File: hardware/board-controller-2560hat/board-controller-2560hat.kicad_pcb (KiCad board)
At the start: 2 copper layers, 3 parts

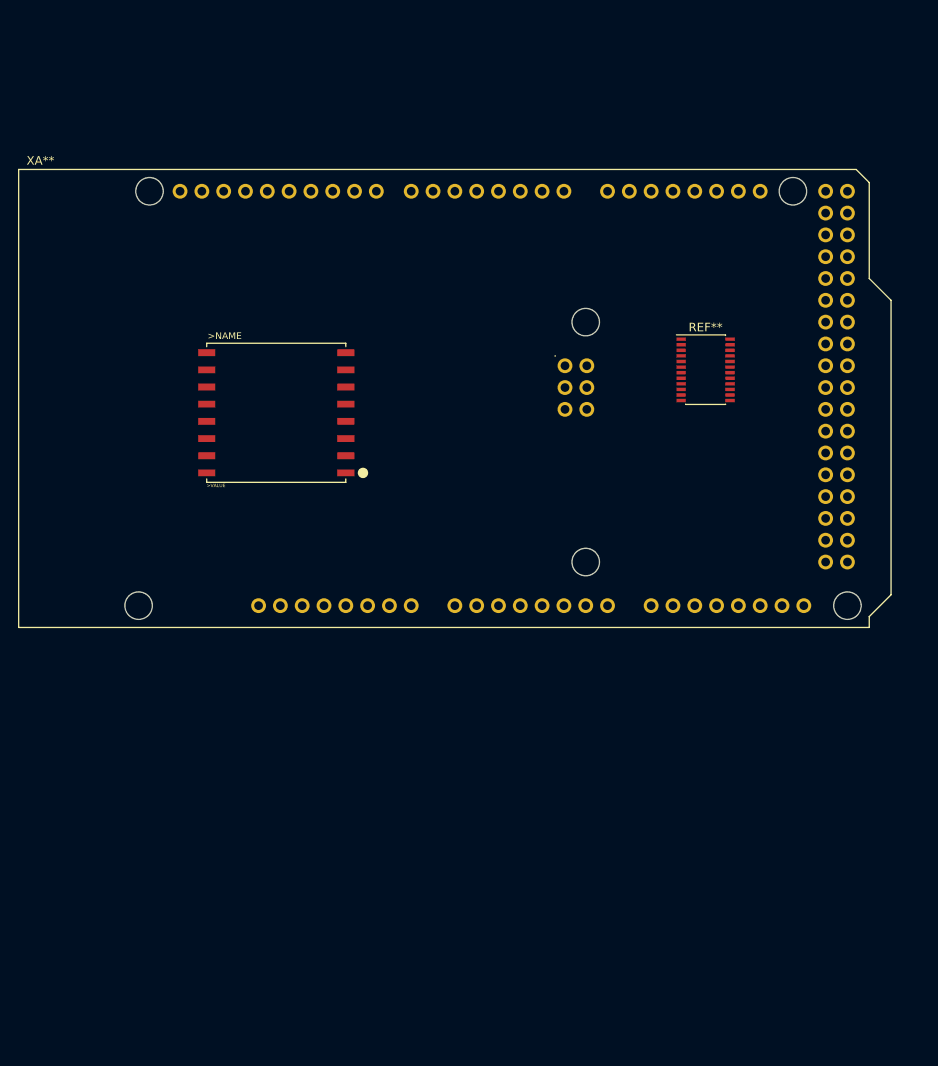
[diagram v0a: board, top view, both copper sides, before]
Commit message: Fixing TFT_ pinouts and rebuilding PCB
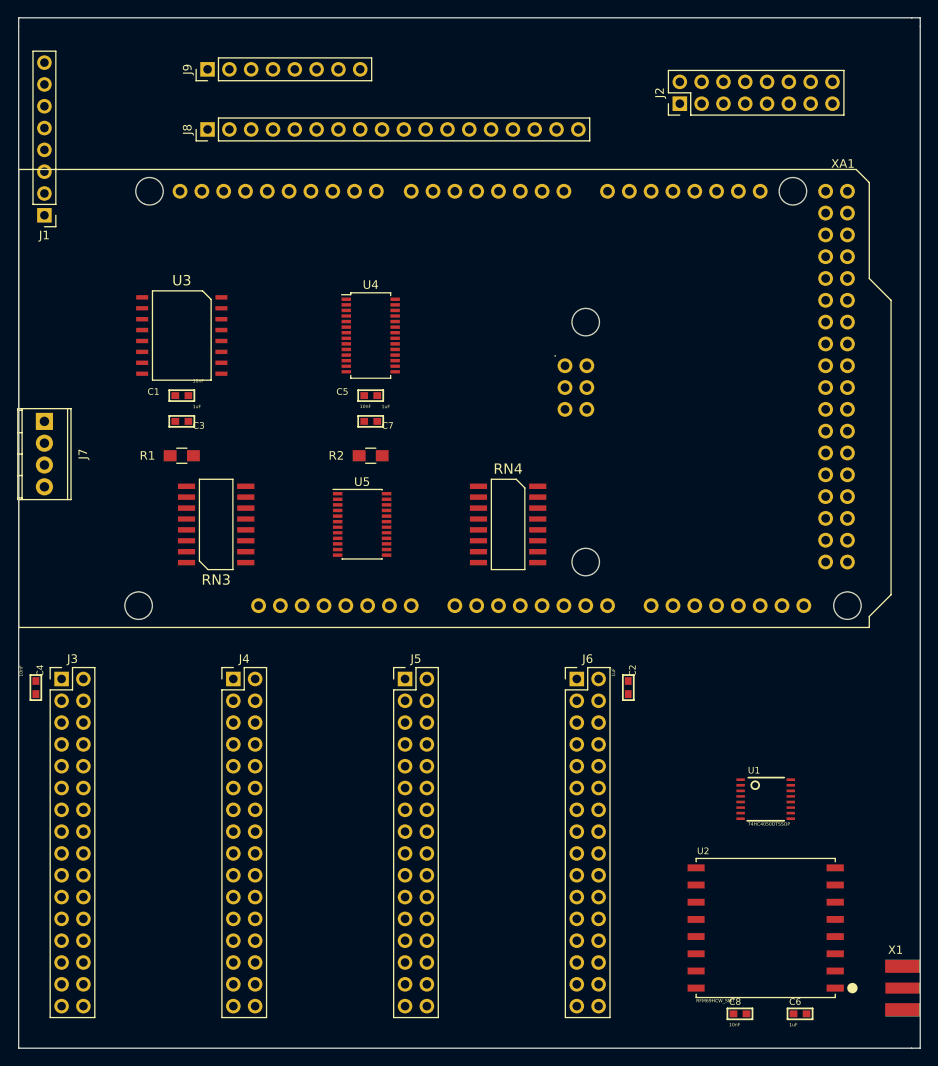
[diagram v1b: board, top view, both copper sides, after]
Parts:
- removed >NAME: >VALUE, Adafruit RFM+LoRa Breakout:RFMHCW_SMT
- removed REF**: TSSOP-24_4.4x7.8mm_Pitch0.65mm, Housings_SSOP:TSSOP-24_4.4x7.8mm_Pitch0.65mm
- removed XA**: Arduino_Mega2560_Shield, Arduino:Arduino_Mega2560_Shield
- added C1: 10nF, _0603, F.Cu at (114.0, 73.0)
- added C2: 1uF, _0603, F.Cu at (166.0, 107.0)
- added C3: 1uF, _0603, F.Cu at (114.0, 76.0)
- added C4: 10nF, _0603, F.Cu at (97.0, 107.0)
- added C5: 10nF, _0603, F.Cu at (136.0, 73.0)
- added C6: 1uF, _0603, F.Cu at (186.0, 145.0)
- added C7: 1uF, _0603, F.Cu at (136.0, 76.0)
- added C8: 10nF, _0603, F.Cu at (179.0, 145.0)
- added J1: CONN_POWER, Pin_Headers:Pin_Header_Straight_1x08_Pitch2.54mm, F.Cu at (98.0, 52.0)
- added J2: CONN_LCD, Pin_Headers:Pin_Header_Straight_2x08_Pitch2.54mm, F.Cu at (172.0, 39.0)
- added J3: CONN_BOARD0, Pin_Headers:Pin_Header_Straight_2x16_Pitch2.54mm, F.Cu at (100.0, 106.0)
- added J4: CONN_BOARD1, Pin_Headers:Pin_Header_Straight_2x16_Pitch2.54mm, F.Cu at (120.0, 106.0)
- added J5: CONN_BOARD2, Pin_Headers:Pin_Header_Straight_2x16_Pitch2.54mm, F.Cu at (140.0, 106.0)
- added J6: CONN_BOARD3, Pin_Headers:Pin_Header_Straight_2x16_Pitch2.54mm, F.Cu at (160.0, 106.0)
- added J7: CONN_SW, Connectors_Terminal_Blocks:TerminalBlock_Pheonix_MPT-2.54mm_4pol, F.Cu at (98.0, 76.0)
- added J8: CONN_KEYLED, Pin_Headers:Pin_Header_Straight_1x18_Pitch2.54mm, F.Cu at (117.0, 42.0)
- added J9: CONN_KEYSW, Pin_Headers:Pin_Header_Straight_1x08_Pitch2.54mm, F.Cu at (117.0, 35.0)
- added R1: 2k2, Resistors_SMD:R_0805_HandSoldering, F.Cu at (114.0, 80.0)
- added R2: 2k2, Resistors_SMD:R_0805_HandSoldering, F.Cu at (136.0, 80.0)
- added RN3: 10k, Housings_SOIC:CA_SOIC_16_5.59x11.18_1.27_Pitch, F.Cu at (118.0, 88.0)
- added RN4: 10k, Housings_SOIC:CA_SOIC_16_5.59x11.18_1.27_Pitch, F.Cu at (152.0, 88.0)
- added U1: 74HC4050DTSSOP, TSSOP16, F.Cu at (182.0, 120.0)
- added U2: RFM69HCW_SMT, RFMHCW_SMT, F.Cu at (182.0, 135.0)
- added U3: PCF8574, Housings_SOIC:CA_SOIC_16_7.5x10.5_1.27_Pitch, F.Cu at (114.0, 66.0)
- added U4: PCA9635PW, Housings_SSOP:TSSOP-28_4.4x9.7mm_Pitch0.65mm, F.Cu at (136.0, 66.0)
- added U5: TCA9548A_TSSOP, Housings_SSOP:TSSOP-24_4.4x7.8mm_Pitch0.65mm, F.Cu at (135.0, 88.0)
- added X1: SMACONNECTOR_EDGE, SMA_EDGELAUNCH, F.Cu at (200.0, 142.0)
- added XA1: Arduino_Mega2560_Shield, Arduino:Arduino_Mega2560_Shield, F.Cu at (95.0, 100.0)
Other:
- board outline added: 105 x 120 mm

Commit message: Adding first autoroute - still need to check nets are correct
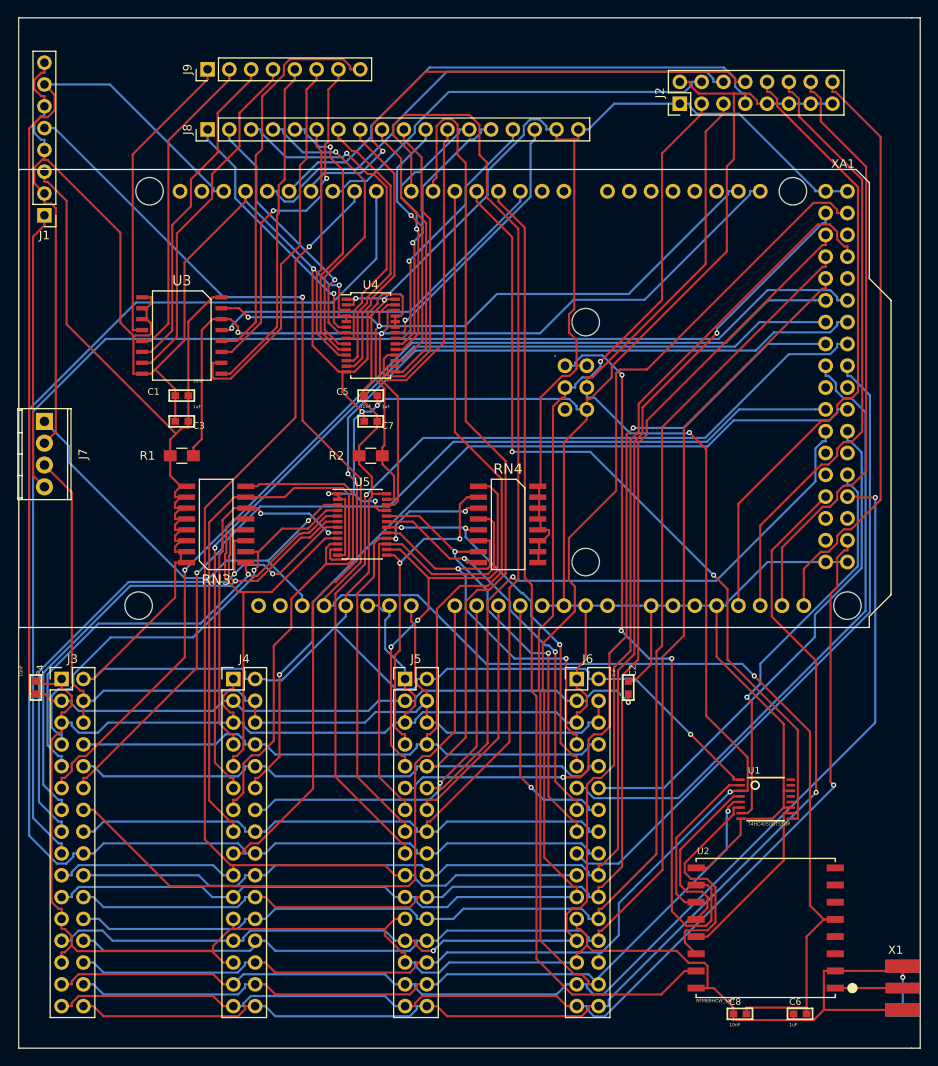
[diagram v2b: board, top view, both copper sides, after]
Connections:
- XA1 pad D11: (no net) -> /LCD_D~C~
- XA1 pad D12: (no net) -> /LCD_~CS~
- XA1 pad D13: (no net) -> /LCD_~RST~
- XA1 pad D50: /LCD_~CS~ -> (no net)
- XA1 pad D51: /LCD_D~C~ -> (no net)
- XA1 pad D52: /LCD_~RST~ -> (no net)
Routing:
- net GND: track 0.00 -> 707.3 mm, vias 0 -> 7
- net +5V: track 0.00 -> 376.2 mm, vias 0 -> 3
- net /DSCL: track 0.00 -> 207.6 mm, vias 0 -> 2
- net /DSDA: track 0.00 -> 190.8 mm, vias 0 -> 2
- net +3V3: track 0.00 -> 186.1 mm, vias 0 -> 2
- net /MA1: track 0.00 -> 177.1 mm
- net /Vref: track 0.00 -> 175.1 mm, vias 0 -> 1
- net /MA0: track 0.00 -> 171.9 mm
- net /DA1: track 0.00 -> 166.8 mm, vias 0 -> 1
- net /FA1: track 0.00 -> 166.2 mm
- net /MCTLB: track 0.00 -> 156.7 mm
- net /F~INT~b0: track 0.00 -> 154.5 mm
- net /FA0: track 0.00 -> 152.5 mm, vias 0 -> 1
- net /DA2: track 0.00 -> 152.4 mm
- net /FA2: track 0.00 -> 152.1 mm
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
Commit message: Completed v0.1 of controller board, added PDFs for boards and datasheet for RFM radio
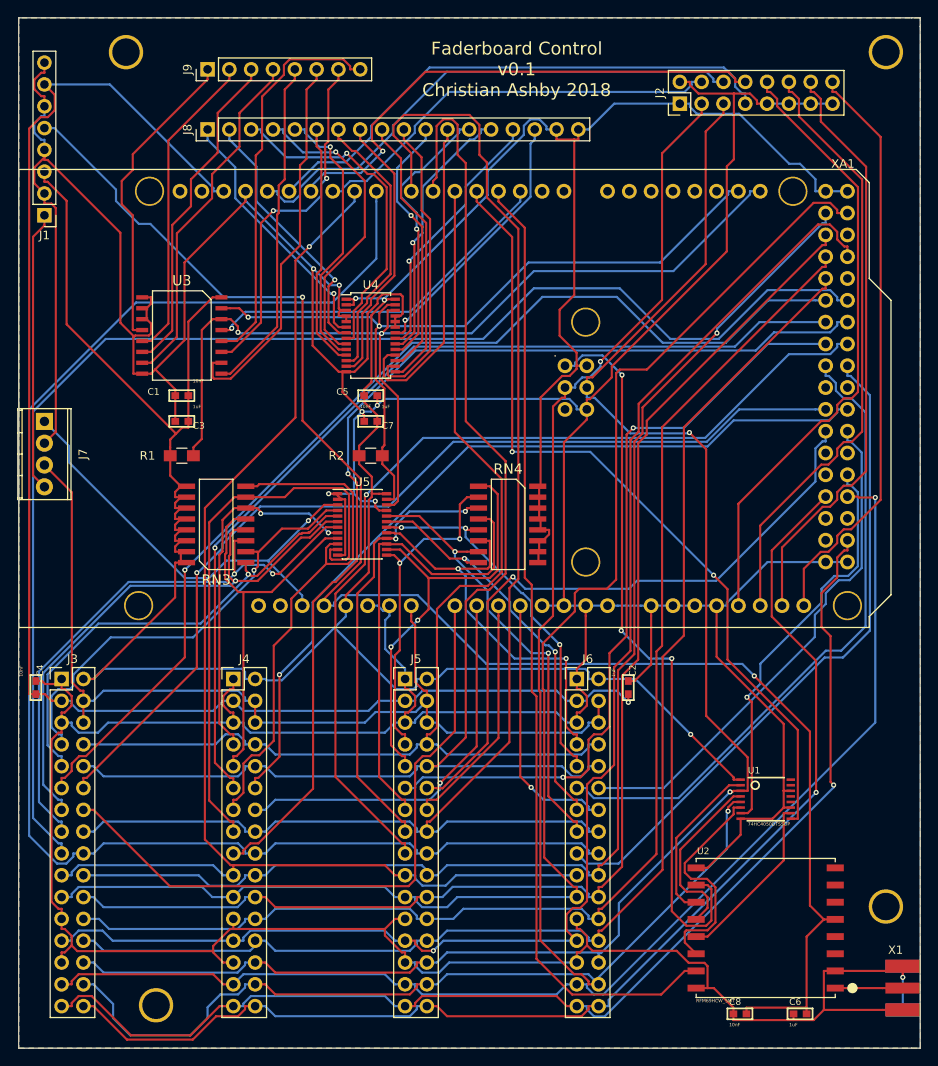
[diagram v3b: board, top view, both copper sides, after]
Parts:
- added REF**: MountingHole_3.2mm_M3_DIN965_Pad, Mounting_Holes:MountingHole_3.2mm_M3_DIN965_Pad, F.Cu at (111.0, 144.0)
- added REF**: MountingHole_3.2mm_M3_DIN965_Pad, Mounting_Holes:MountingHole_3.2mm_M3_DIN965_Pad, F.Cu at (196.0, 132.5)
- added REF**: MountingHole_3.2mm_M3_DIN965_Pad, Mounting_Holes:MountingHole_3.2mm_M3_DIN965_Pad, F.Cu at (107.5, 33.0)
- added REF**: MountingHole_3.2mm_M3_DIN965_Pad, Mounting_Holes:MountingHole_3.2mm_M3_DIN965_Pad, F.Cu at (196.0, 33.0)
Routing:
- net /DSCL: track 207.6 -> 213.2 mm
- net /F~INT~b0: track 154.5 -> 159.4 mm
- net /F~INT~a0: track 119.7 -> 124.1 mm
- net /D~CS~: track 135.2 -> 138.9 mm
- net /D~RST~: track 138.8 -> 141.1 mm
- net +5V: track 376.2 -> 377.8 mm
- net /FA1: track 166.2 -> 167.5 mm
- net /F~INT~b3: track 76.8 -> 78.0 mm
- net /KEY_COL0: track 35.0 -> 36.1 mm
- net /F~INT~a3: track 74.6 -> 75.6 mm
- net /RFM_~RST~_5v: track 46.7 -> 47.7 mm
- net +3V3: track 186.1 -> 186.8 mm
- net /BSEL2: track 76.7 -> 77.5 mm
- net /BSEL3: track 59.6 -> 60.3 mm
- added copper zone on B.Cu, net GND
- added copper zone on F.Cu, net GND
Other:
- board text added: "Faderboard Control v0.1 Christian Ashby 2018"
